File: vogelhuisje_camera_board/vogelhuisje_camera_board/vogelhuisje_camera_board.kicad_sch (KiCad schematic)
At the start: 1 part, among them J1 Conn_01x19_Female

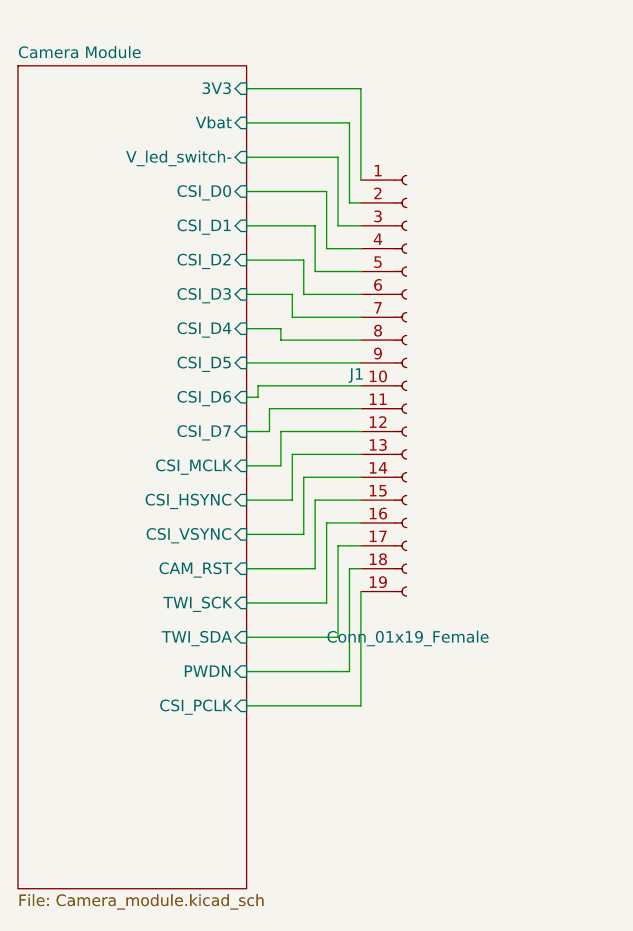
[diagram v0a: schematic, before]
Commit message: Kicad Changes Tadjiro
Board now supports 3 lipo cells and a motion sensor.
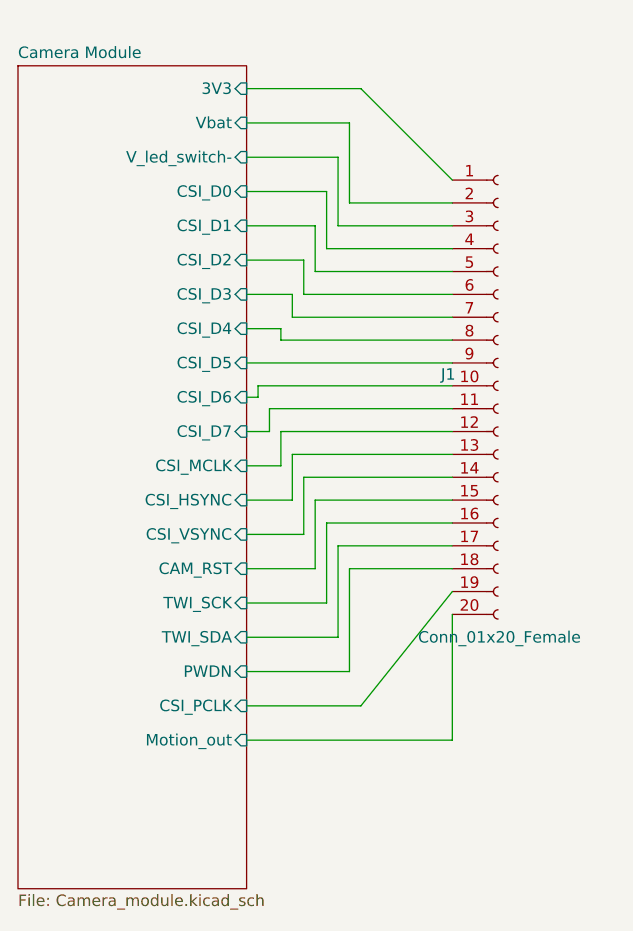
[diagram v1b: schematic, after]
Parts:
- J1: value Conn_01x19_Female -> Conn_01x20_Female; footprint Connector_PinHeader_2.54mm:PinHeader_1x19_P2.54mm_Vertical -> Connector_PinHeader_2.54mm:PinHeader_1x20_P2.54mm_Vertical; symbol Connector:Conn_01x19_Female -> Connector:Conn_01x20_Female
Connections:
- new net Camera Module/Motion_out: J1.20 (Pin_20)
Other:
- sheet Camera Module ports: added Motion_out; removed none

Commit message: Updated Camera Board
Moved capacitors close to LDO output, corrected capacitor values and ported ground from the main board.
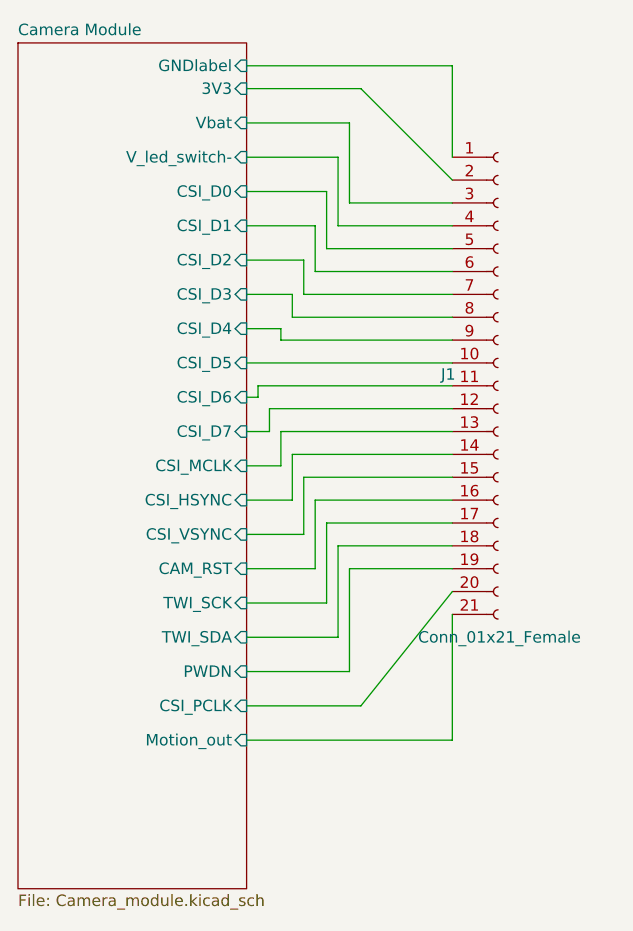
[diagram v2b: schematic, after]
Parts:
- J1: value Conn_01x20_Female -> Conn_01x21_Female; footprint Connector_PinHeader_2.54mm:PinHeader_1x20_P2.54mm_Vertical -> Connector_PinHeader_2.54mm:PinHeader_1x21_P2.54mm_Vertical; symbol Connector:Conn_01x20_Female -> Connector:Conn_01x21_Female
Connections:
- net Camera Module/3V3: now also J1.2 (Pin_2); no longer J1.1 (Pin_1)
- net Camera Module/CAM_RST: now also J1.16 (Pin_16); no longer J1.15 (Pin_15)
- net Camera Module/CSI_D0: now also J1.5 (Pin_5); no longer J1.4 (Pin_4)
- net Camera Module/CSI_D1: now also J1.6 (Pin_6); no longer J1.5 (Pin_5)
- net Camera Module/CSI_D2: now also J1.7 (Pin_7); no longer J1.6 (Pin_6)
- net Camera Module/CSI_D3: now also J1.8 (Pin_8); no longer J1.7 (Pin_7)
- net Camera Module/CSI_D4: now also J1.9 (Pin_9); no longer J1.8 (Pin_8)
- net Camera Module/CSI_D5: now also J1.10 (Pin_10); no longer J1.9 (Pin_9)
- net Camera Module/CSI_D6: now also J1.11 (Pin_11); no longer J1.10 (Pin_10)
- net Camera Module/CSI_D7: now also J1.12 (Pin_12); no longer J1.11 (Pin_11)
- net Camera Module/CSI_HSYNC: now also J1.14 (Pin_14); no longer J1.13 (Pin_13)
- net Camera Module/CSI_MCLK: now also J1.13 (Pin_13); no longer J1.12 (Pin_12)
- net Camera Module/CSI_PCLK: now also J1.20 (Pin_20); no longer J1.19 (Pin_19)
- net Camera Module/CSI_VSYNC: now also J1.15 (Pin_15); no longer J1.14 (Pin_14)
- net Camera Module/Motion_out: now also J1.21 (Pin_21); no longer J1.20 (Pin_20)
- net Camera Module/PWDN: now also J1.19 (Pin_19); no longer J1.18 (Pin_18)
- net Camera Module/TWI_SCK: now also J1.17 (Pin_17); no longer J1.16 (Pin_16)
- net Camera Module/TWI_SDA: now also J1.18 (Pin_18); no longer J1.17 (Pin_17)
- net Camera Module/V_led_switch-: now also J1.4 (Pin_4); no longer J1.3 (Pin_3)
- net Camera Module/Vbat: now also J1.3 (Pin_3); no longer J1.2 (Pin_2)
- new net Camera Module/GNDlabel: J1.1 (Pin_1)
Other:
- sheet Camera Module ports: added GNDlabel; removed none
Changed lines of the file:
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@@
+    (stroke (width 0) (type default) (color 0 0 0 0))
+  )
+  (wire (pts (xy 115.57 55.88) (xy 138.43 55.88))
     (stroke (width 0) (type default) (color 0 0 0 0))
   )
@@
     (stroke (width 0) (type default) (color 0 0 0 0))
   )
+  (wire (pts (xy 138.43 55.88) (xy 138.43 66.04))
+    (stroke (width 0) (type default) (color 0 0 0 0))
+  )
   (wire (pts (xy 119.38 96.52) (xy 138.43 96.52))
     (stroke (width 0) (type default) (color 0 0 0 0))
@@
     (stroke (width 0) (type default) (color 0 0 0 0))
   )
-  (symbol (lib_id "Connector:Conn_01x20_Female") (at 143.51 91.44 0) (unit 1)
+  (symbol (lib_id "Connector:Conn_01x21_Female") (at 143.51 91.44 0) (unit 1)
     (in_bom yes) (on_board yes)
     (property "Reference" "J1" (id 0) (at 137.16 90.17 0)
       (effects (font (size 1.27 1.27)) (justify left))
     )
-    (property "Value" "Conn_01x20_Female" (id 1) (at 134.62 119.38 0)
+    (property "Value" "Conn_01x21_Female" (id 1) (at 134.62 119.38 0)
       (effects (font (size 1.27 1.27)) (justify left))
     )
-    (property "Footprint" "Connector_PinHeader_2.54mm:PinHeader_1x20_P2.54mm_Vertical" (id 2) (at 143.51 91.44 0)
+    (property "Footprint" "Connector_PinHeader_2.54mm:PinHeader_1x21_P2.54mm_Vertical" (id 2) (at 143.51 91.44 0)
       (effects (font (size 1.27 1.27)) hide)
     )
@@
     (pin "2")
     (pin "20")
+    (pin "21")
     (pin "3")
     (pin "4")
@@
     (pin "9")
   )
-  (sheet (at 90.17 55.88) (size 25.4 91.44) (fields_autoplaced)
+  (sheet (at 90.17 53.34) (size 25.4 93.98) (fields_autoplaced)
     (stroke (width 0) (type solid) (color 0 0 0 0))
     (fill (color 0 0 0 0.0000))
-    (property "Sheet name" "Camera Module" (id 0) (at 90.17 55.1684 0)
+    (property "Sheet name" "Camera Module" (id 0) (at 90.17 52.6284 0)
       (effects (font (size 1.27 1.27)) (justify left bottom))
     )
@@
     )
     (pin "Motion_out" input (at 115.57 130.81 0)
+      (effects (font (size 1.27 1.27)) (justify right))
+    )
+    (pin "GNDlabel" input (at 115.57 55.88 0)
       (effects (font (size 1.27 1.27)) (justify right))
     )
@@
       (reference "100n1") (unit 1) (value "100nF") (footprint "Capacitor_THT:C_Axial_L5.1mm_D3.1mm_P7.50mm_Horizontal")
     )
+    (path "/c75750c0-c5ef-4d26-9b8b-80f441dd56ec/00000000-0000-0000-0000-00006271f0d7"
+      (reference "C1u1") (unit 1) (value "1u") (footprint "Capacitor_THT:C_Axial_L5.1mm_D3.1mm_P7.50mm_Horizontal")
+    )
     (path "/c75750c0-c5ef-4d26-9b8b-80f441dd56ec/00000000-0000-0000-0000-00006271f8fb"
-      (reference "C10u1") (unit 1) (value "10u") (footprint "Capacitor_THT:C_Axial_L5.1mm_D3.1mm_P7.50mm_Horizontal")
+      (reference "C1u2") (unit 1) (value "1u") (footprint "Capacitor_THT:C_Axial_L5.1mm_D3.1mm_P7.50mm_Horizontal")
     )
     (path "/c75750c0-c5ef-4d26-9b8b-80f441dd56ec/00000000-0000-0000-0000-00006271e5c1"
-      (reference "C10u2") (unit 1) (value "10u") (footprint "Capacitor_THT:C_Axial_L5.1mm_D3.1mm_P7.50mm_Horizontal")
-    )
-    (path "/c75750c0-c5ef-4d26-9b8b-80f441dd56ec/00000000-0000-0000-0000-00006271f0d7"
-      (reference "C10u3") (unit 1) (value "10u") (footprint "Capacitor_THT:C_Axial_L5.1mm_D3.1mm_P7.50mm_Horizontal")
-    )
-    (path "/c75750c0-c5ef-4d26-9b8b-80f441dd56ec/00000000-0000-0000-0000-00006271f4d9"
-      (reference "C100n2") (unit 1) (value "100n") (footprint "Capacitor_THT:C_Axial_L5.1mm_D3.1mm_P7.50mm_Horizontal")
-    )
-    (path "/c75750c0-c5ef-4d26-9b8b-80f441dd56ec/00000000-0000-0000-0000-00006271fd3d"
-      (reference "C100n3") (unit 1) (value "100n") (footprint "Capacitor_THT:C_Axial_L5.1mm_D3.1mm_P7.50mm_Horizontal")
+      (reference "C1u3") (unit 1) (value "1u") (footprint "Capacitor_THT:C_Axial_L5.1mm_D3.1mm_P7.50mm_Horizontal")
     )
     (path "/c75750c0-c5ef-4d26-9b8b-80f441dd56ec/00000000-0000-0000-0000-0000626e8633"
@@
     )
     (path "/09540e8b-37cf-40f4-841d-7605671ea021"
-      (reference "J1") (unit 1) (value "Conn_01x20_Female") (footprint "Connector_PinHeader_2.54mm:PinHeader_1x20_P2.54mm_Vertical")
+      (reference "J1") (unit 1) (value "Conn_01x21_Female") (footprint "Connector_PinHeader_2.54mm:PinHeader_1x21_P2.54mm_Vertical")
     )
     (path "/c75750c0-c5ef-4d26-9b8b-80f441dd56ec/00000000-0000-0000-0000-0000626f059a"
@@
     )
     (path "/c75750c0-c5ef-4d26-9b8b-80f441dd56ec/00000000-0000-0000-0000-0000626ddee8"
-      (reference "Q2") (unit 1) (value "Q_NMOS_DSG") (footprint "Package_TO_SOT_THT:TO-92L_Inline")
+      (reference "Q2") (unit 1) (value "Q_NMOS_DGS") (footprint "Package_TO_SOT_THT:TO-92L_Inline")
     )
     (path "/c75750c0-c5ef-4d26-9b8b-80f441dd56ec/00000000-0000-0000-0000-0000626f76bd"
@@
     )
     (path "/c75750c0-c5ef-4d26-9b8b-80f441dd56ec/00000000-0000-0000-0000-0000626f28f9"
-      (reference "R3") (unit 1) (value "R") (footprint "Resistor_THT:R_Axial_DIN0207_L6.3mm_D2.5mm_P10.16mm_Horizontal")
+      (reference "R33O1") (unit 1) (value "33Ohm") (footprint "Resistor_THT:R_Axial_DIN0207_L6.3mm_D2.5mm_P10.16mm_Horizontal")
     )
     (path "/c75750c0-c5ef-4d26-9b8b-80f441dd56ec/00000000-0000-0000-0000-0000626da198"
-      (reference "R4") (unit 1) (value "R") (footprint "Resistor_THT:R_Axial_DIN0207_L6.3mm_D2.5mm_P10.16mm_Horizontal")
+      (reference "R100k1") (unit 1) (value "100kOhm") (footprint "Resistor_THT:R_Axial_DIN0207_L6.3mm_D2.5mm_P10.16mm_Horizontal")
     )
     (path "/c75750c0-c5ef-4d26-9b8b-80f441dd56ec/00000000-0000-0000-0000-00006271743c"
